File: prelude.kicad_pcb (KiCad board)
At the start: 2 copper layers, 80 x 60 mm, 41 parts, among them J1 CONN_01X50, J2 USB_C, J3 Conn_01x04, J4 Conn_01x08, SW1 SW_Push, U1 LM3671MF-3.3, U2 STM32F411RETx, U3 AP5724, Y1 16MHz

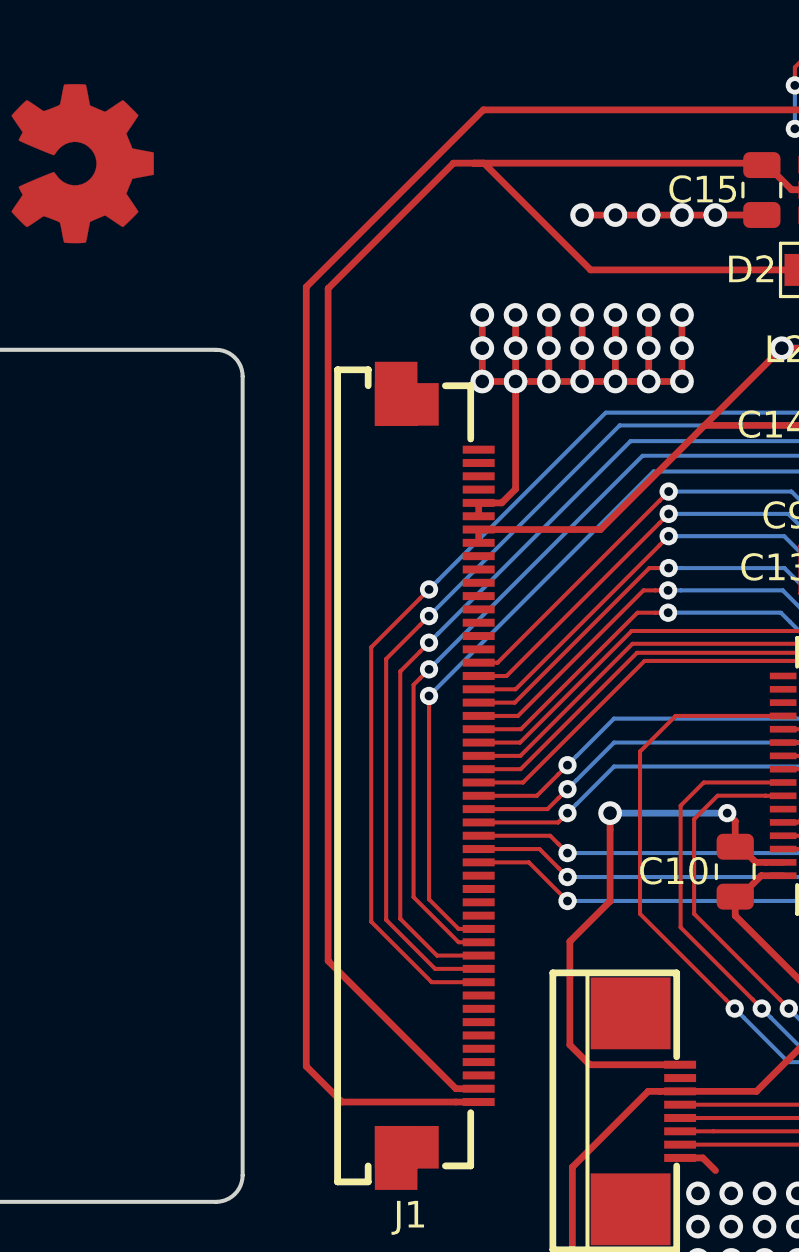
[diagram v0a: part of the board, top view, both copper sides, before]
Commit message: Updates layout after importing latest netlist with changes in schematic.
Moved LED_A trace to be more like LED_K on its way to J1, recalculates fill zones.
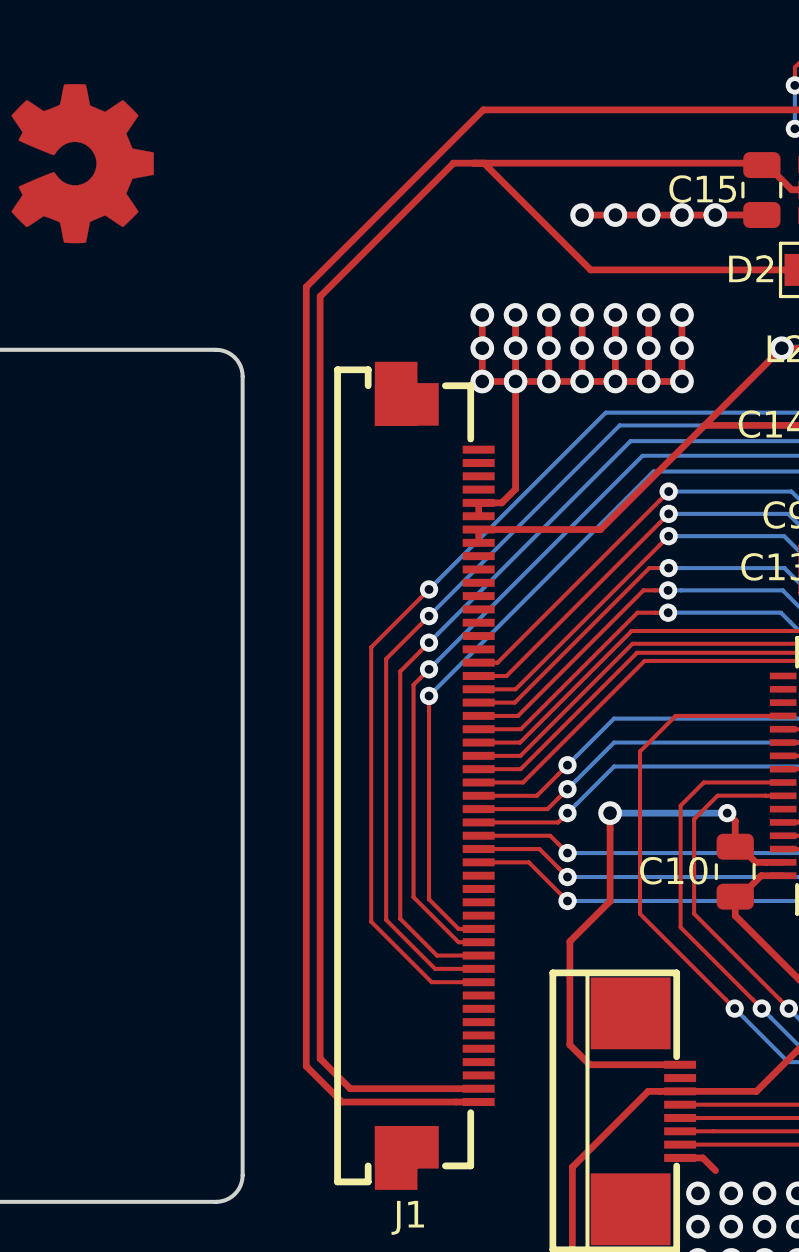
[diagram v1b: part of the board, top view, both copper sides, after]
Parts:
- C1, C2: value 8p -> 8pF
- C10, C12, C3, C5, C8, C9: value 100n -> 100nF
- C11: value 22u -> 22uF
- C13: value 4.7u LowESR < 1Ω Ceramic -> 4.7uF LowESR < 1Ω Ceramic
- C6: value 1u -> 1uF
- C7: value 10u -> 10uF
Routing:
- net /LED_A: track 67.7 -> 70.3 mm
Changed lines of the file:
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@@
       (effects (font (size 1 1) (thickness 0.15)))
     )
-    (fp_text value 8p (at 0 1.65 90) (layer F.Fab)
+    (fp_text value 8pF (at 0 1.65 90) (layer F.Fab)
       (effects (font (size 1 1) (thickness 0.15)))
     )
@@
       (effects (font (size 1 1) (thickness 0.15)))
     )
-    (fp_text value 8p (at 0 1.65 270) (layer F.Fab)
+    (fp_text value 8pF (at 0 1.65 270) (layer F.Fab)
       (effects (font (size 1 1) (thickness 0.15)))
     )
@@
       (effects (font (size 1 1) (thickness 0.15)))
     )
-    (fp_text value 100n (at 0 1.65) (layer F.Fab)
+    (fp_text value 100nF (at 0 1.65) (layer F.Fab)
       (effects (font (size 1 1) (thickness 0.15)))
     )
@@
       (effects (font (size 1 1) (thickness 0.15)))
     )
-    (fp_text value 100n (at 0 1.65 270) (layer F.Fab)
+    (fp_text value 100nF (at 0 1.65 270) (layer F.Fab)
       (effects (font (size 1 1) (thickness 0.15)))
     )
@@
       (effects (font (size 1 1) (thickness 0.15)))
     )
-    (fp_text value 1u (at 0 1.65 270) (layer F.Fab)
+    (fp_text value 1uF (at 0 1.65 270) (layer F.Fab)
       (effects (font (size 1 1) (thickness 0.15)))
     )
@@
       (effects (font (size 1 1) (thickness 0.15)))
     )
-    (fp_text value 10u (at 0 1.65) (layer F.Fab)
+    (fp_text value 10uF (at 0 1.65) (layer F.Fab)
       (effects (font (size 1 1) (thickness 0.15)))
     )
@@
       (effects (font (size 1 1) (thickness 0.15)))
     )
-    (fp_text value 100n (at 0 1.65) (layer F.Fab)
+    (fp_text value 100nF (at 0 1.65) (layer F.Fab)
       (effects (font (size 1 1) (thickness 0.15)))
     )
@@
       (effects (font (size 1 1) (thickness 0.15)))
     )
-    (fp_text value 100n (at 0 1.65) (layer F.Fab)
+    (fp_text value 100nF (at 0 1.65) (layer F.Fab)
       (effects (font (size 1 1) (thickness 0.15)))
     )
@@
       (effects (font (size 1 1) (thickness 0.15)))
     )
-    (fp_text value 100n (at 0 1.65 90) (layer F.Fab)
+    (fp_text value 100nF (at 0 1.65 90) (layer F.Fab)
       (effects (font (size 1 1) (thickness 0.15)))
     )
@@
       (effects (font (size 1 1) (thickness 0.15)))
     )
-    (fp_text value 22u (at 0 1.65 90) (layer F.Fab)
+    (fp_text value 22uF (at 0 1.65 90) (layer F.Fab)
       (effects (font (size 1 1) (thickness 0.15)))
     )
@@
       (effects (font (size 1 1) (thickness 0.15)))
     )
-    (fp_text value 100n (at 0 1.65) (layer F.Fab)
+    (fp_text value 100nF (at 0 1.65) (layer F.Fab)
       (effects (font (size 1 1) (thickness 0.15)))
     )
@@
       (effects (font (size 1 1) (thickness 0.15)))
     )
-    (fp_text value "4.7u  LowESR < 1Ω Ceramic" (at 0 1.65 180) (layer F.Fab)
+    (fp_text value "4.7uF  LowESR < 1Ω Ceramic" (at 0 1.65 180) (layer F.Fab)
       (effects (font (size 1 1) (thickness 0.15)))
     )
@@
   (segment (start 160.97 47.99) (end 161.2 47.99) (width 0.254) (layer Top) (net 6))
   (segment (start 161.2 47.99) (end 161.9 47.99) (width 0.254) (layer Top) (net 6))
-  (segment (start 147.92 46.99) (end 148.68 46.99) (width 0.254) (layer Top) (net 6))
-  (segment (start 143.21 51.7) (end 147.92 46.99) (width 0.254) (layer Top) (net 6))
-  (segment (start 143.21 76.949) (end 143.21 51.7) (width 0.254) (layer Top) (net 6))
-  (segment (start 148.865 81.75) (end 148.011 81.75) (width 0.254) (layer Top) (net 6))
-  (segment (start 148.011 81.75) (end 143.21 76.949) (width 0.254) (layer Top) (net 6))
   (segment (start 149.06 46.99) (end 148.68 46.99) (width 0.254) (layer Top) (net 6))
   (segment (start 160.8 51) (end 153.07 51) (width 0.254) (layer Top) (net 6))
   (segment (start 153.07 51) (end 149.06 46.99) (width 0.254) (layer Top) (net 6))
+  (segment (start 147.92 46.99) (end 148.68 46.99) (width 0.254) (layer Top) (net 6))
+  (segment (start 142.91 52) (end 147.92 46.99) (width 0.254) (layer Top) (net 6))
+  (segment (start 142.91 80.62) (end 142.91 52) (width 0.254) (layer Top) (net 6))
+  (segment (start 148.865 81.75) (end 144.04 81.75) (width 0.254) (layer Top) (net 6))
+  (segment (start 144.04 81.75) (end 142.91 80.62) (width 0.254) (layer Top) (net 6))
   (segment (start 170.15 55.09) (end 170.23 55.01) (width 0.1524) (layer Top) (net 7))
   (segment (start 170.2625 55) (end 170.2 54.9375) (width 0.1524) (layer Top) (net 7))

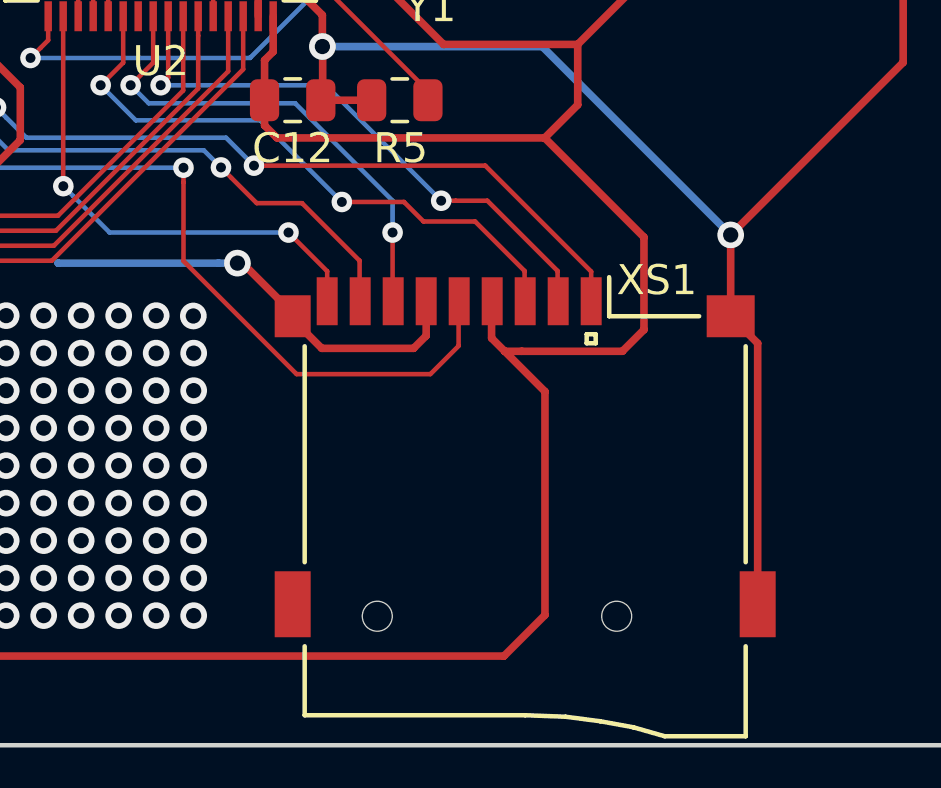
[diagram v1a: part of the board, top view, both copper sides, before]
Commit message: Minor clean up of tracks
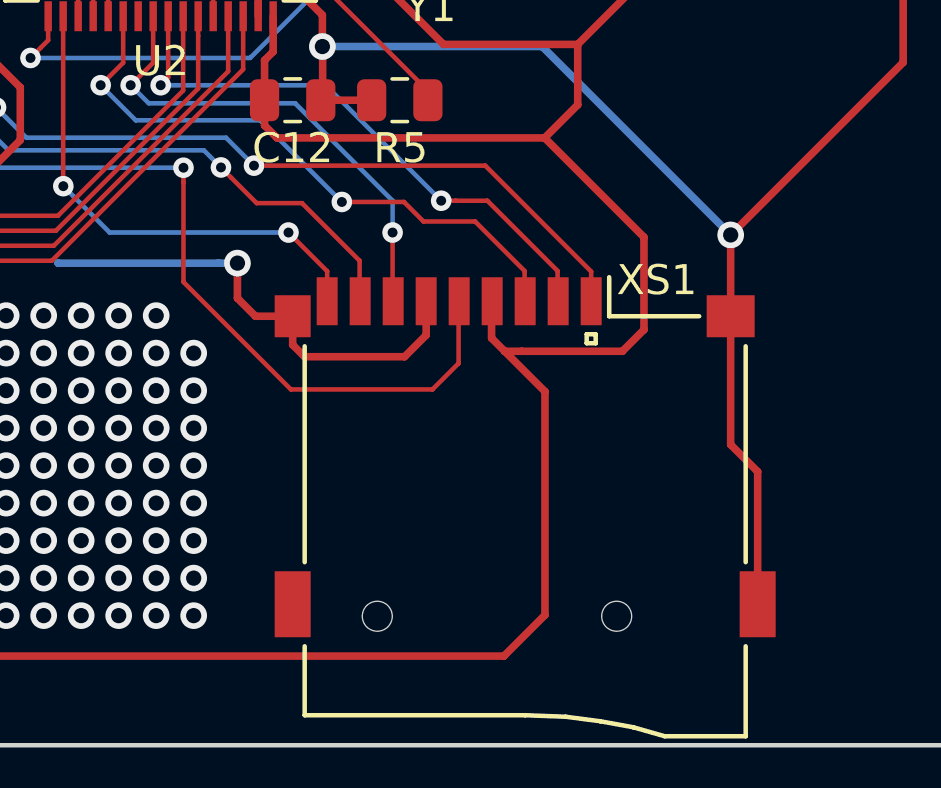
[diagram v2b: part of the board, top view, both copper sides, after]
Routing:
- net GND: track 348.4 -> 350.2 mm, vias 225 -> 224
- net /SDIO_CLK: track 42.4 -> 43.6 mm
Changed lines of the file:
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@@
     (thickness 1.6)
     (drawings 24)
-    (tracks 1099)
+    (tracks 1102)
     (zones 0)
     (modules 41)
@@
   (segment (start 185 85.7) (end 185 82.99) (width 0.254) (layer Top) (net 2))
   (via (at 185 82.99) (size 0.889) (drill 0.508) (layers Top Bottom) (net 2))
-  (segment (start 185.9 95.3) (end 185.9 86.6) (width 0.254) (layer Top) (net 2))
-  (segment (start 185.9 86.6) (end 185 85.7) (width 0.254) (layer Top) (net 2))
   (segment (start 171.4 78.5) (end 171.4 76.72) (width 0.254) (layer Top) (net 2))
   (via (at 171.39 76.71) (size 0.889) (drill 0.508) (layers Top Bottom) (net 2))
@@
   (via (at 179.9 49.39) (size 0.889) (drill 0.508) (layers Top Bottom) (net 2))
   (segment (start 170.4 85.8) (end 170.4 85.7) (width 0.254) (layer Top) (net 2))
-  (segment (start 171.37 86.77) (end 170.4 85.8) (width 0.254) (layer Top) (net 2))
-  (segment (start 174.43 86.77) (end 171.37 86.77) (width 0.254) (layer Top) (net 2))
-  (segment (start 174.85 85.2) (end 174.85 86.35) (width 0.254) (layer Top) (net 2))
-  (segment (start 174.85 86.35) (end 174.43 86.77) (width 0.254) (layer Top) (net 2))
   (segment (start 178.3 72.4125) (end 178.3 70.5875) (width 0.254) (layer Top) (net 2))
   (segment (start 178.3 70.5875) (end 180.2975 70.5875) (width 0.254) (layer Top) (net 2))
@@
   (via (at 167.1 86.93) (size 0.889) (drill 0.508) (layers Top Bottom) (net 2))
   (via (at 168.558617 83.930008) (size 0.889) (drill 0.508) (layers Top Bottom) (net 2))
-  (segment (start 170.4 85.6) (end 168.730008 83.930008) (width 0.254) (layer Top) (net 2))
   (segment (start 168.730008 83.930008) (end 168.558617 83.930008) (width 0.254) (layer Top) (net 2))
   (segment (start 170.4 85.7) (end 170.4 85.6) (width 0.254) (layer Top) (net 2))
@@
   (segment (start 162.580008 83.930008) (end 167.93 83.930008) (width 0.254) (layer Bottom) (net 2))
   (segment (start 162.58 83.93) (end 162.580008 83.930008) (width 0.254) (layer Bottom) (net 2))
-  (via (at 167.088388 85.691612) (size 0.889) (drill 0.508) (layers Top Bottom) (net 2))
   (segment (start 148.865 59.75) (end 148.865 60.25) (width 0.254) (layer Top) (net 2))
   (segment (start 192.31 51) (end 192.31 49.925) (width 0.254) (layer Top) (net 2))
@@
   (segment (start 197.5 61.25) (end 197.5 60) (width 0.254) (layer Top) (net 2))
   (segment (start 195 63.75) (end 195 62.5) (width 0.254) (layer Top) (net 2))
+  (segment (start 185.9 90.88) (end 185.9 95.3) (width 0.254) (layer Top) (net 2))
+  (segment (start 185 85.7) (end 185 89.98) (width 0.254) (layer Top) (net 2))
+  (segment (start 185 89.98) (end 185.9 90.88) (width 0.254) (layer Top) (net 2))
+  (segment (start 170.4 85.7) (end 169.16 85.7) (width 0.254) (layer Top) (net 2))
+  (segment (start 168.558617 85.098617) (end 168.558617 83.930008) (width 0.254) (layer Top) (net 2))
+  (segment (start 169.16 85.7) (end 168.558617 85.098617) (width 0.254) (layer Top) (net 2))
+  (segment (start 174.85 86.33) (end 174.85 85.2) (width 0.254) (layer Top) (net 2))
+  (segment (start 174.13 87.05) (end 174.85 86.33) (width 0.254) (layer Top) (net 2))
+  (segment (start 170.796 87.05) (end 174.13 87.05) (width 0.254) (layer Top) (net 2))
+  (segment (start 170.4 85.7) (end 170.4 86.654) (width 0.254) (layer Top) (net 2))
+  (segment (start 170.4 86.654) (end 170.796 87.05) (width 0.254) (layer Top) (net 2))
   (segment (start 178 68.65) (end 176 68.65) (width 0.1524) (layer Top) (net 3))
   (segment (start 176 68.65) (end 175 69.65) (width 0.1524) (layer Top) (net 3))
@@
   (via (at 166.76 80.75) (size 0.6858) (drill 0.3302) (layers Top Bottom) (net 42))
   (segment (start 166.76 81.234933) (end 166.76 80.75) (width 0.1524) (layer Top) (net 42))
-  (segment (start 166.76 83.86) (end 166.76 81.234933) (width 0.1524) (layer Top) (net 42))
-  (segment (start 170.53 87.63) (end 166.76 83.86) (width 0.1524) (layer Top) (net 42))
-  (segment (start 174.99 87.63) (end 170.53 87.63) (width 0.1524) (layer Top) (net 42))
-  (segment (start 175.93 84.64) (end 175.93 86.69) (width 0.1524) (layer Top) (net 42))
-  (segment (start 175.93 86.69) (end 174.99 87.63) (width 0.1524) (layer Top) (net 42))
+  (segment (start 166.76 84.56) (end 166.76 81.234933) (width 0.1524) (layer Top) (net 42))
+  (segment (start 170.34 88.14) (end 166.76 84.56) (width 0.1524) (layer Top) (net 42))
+  (segment (start 175.06 88.14) (end 170.34 88.14) (width 0.1524) (layer Top) (net 42))
+  (segment (start 175.93 84.64) (end 175.93 87.27) (width 0.1524) (layer Top) (net 42))
+  (segment (start 175.93 87.27) (end 175.06 88.14) (width 0.1524) (layer Top) (net 42))
   (via (at 172.039121 81.891335) (size 0.6858) (drill 0.3302) (layers Top Bottom) (net 43))
   (segment (start 172.040456 81.89) (end 172.039121 81.891335) (width 0.1524) (layer Top) (net 43))
